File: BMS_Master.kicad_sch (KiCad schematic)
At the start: 70 parts, among them J1 PWR, J2 PROG, J3 BMS_M_OUT, J4 BMS_M_IN, J5 CAN, Q1 BC807, SW1 SW_SPST, U1 AP2204K-ADJ, U2 AP2204K-ADJ, U3 STM32F103C8Tx, U4 BQ79600-Q1, U5 SN65HVD256D, Y1 8M, Y2 32.768k

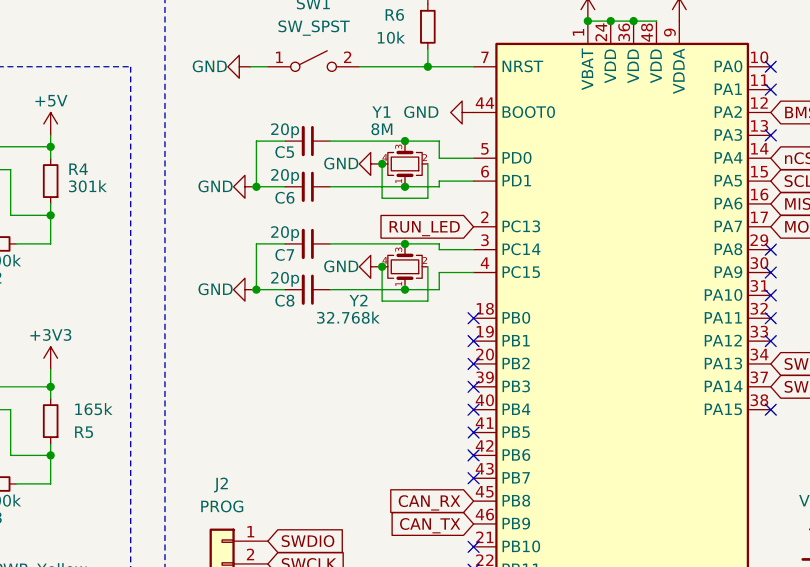
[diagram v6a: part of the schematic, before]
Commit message: Fix crystal pinout connection
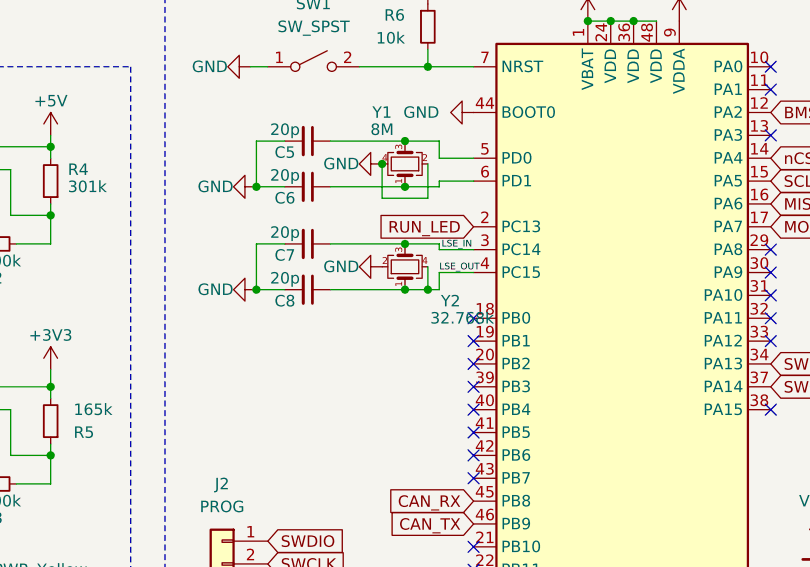
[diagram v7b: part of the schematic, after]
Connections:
- net GND: no longer Y2.4
- net LSE_OUT: now reaches C8.1, U3.4 (PC15), Y2.1
- net LSE_OUT: now also Y2.4
- net LSE_IN: now reaches C7.1, U3.3 (PC14), Y2.3
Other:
- moved on the sheet: Y2
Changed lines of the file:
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@@
   (junction (at 217.17 55.88) (diameter 0) (color 0 0 0 0)
   )
+  (junction (at 98.425 55.88) (diameter 0) (color 0 0 0 0)
+  )
   (junction (at 43.815 50.8) (diameter 0) (color 0 0 0 0)
   )
@@
   )
   (junction (at 219.71 135.89) (diameter 0) (color 0 0 0 0)
-  )
-  (junction (at 93.345 53.34) (diameter 0) (color 0 0 0 0)
   )
   (junction (at 204.47 71.12) (diameter 0) (color 0 0 0 0)
@@
     (stroke (width 0) (type default))
   )
-  (wire (pts (xy 95.885 55.88) (xy 99.695 55.88))
+  (wire (pts (xy 95.885 55.88) (xy 98.425 55.88))
     (stroke (width 0) (type default))
   )
@@
     (stroke (width 0) (type default))
   )
+  (wire (pts (xy 98.425 53.34) (xy 98.425 55.88))
+    (stroke (width 0) (type default))
+  )
   (wire (pts (xy 99.695 51.435) (xy 103.505 51.435))
     (stroke (width 0) (type default))
@@
     (stroke (width 0) (type default))
   )
+  (wire (pts (xy 98.425 55.88) (xy 99.695 55.88))
+    (stroke (width 0) (type default))
+  )
   (wire (pts (xy 106.68 162.56) (xy 106.68 164.465))
     (stroke (width 0) (type default))
@@
     (stroke (width 0) (type default))
   )
-  (wire (pts (xy 98.425 57.15) (xy 93.345 57.15))
-    (stroke (width 0) (type default))
-  )
   (wire (pts (xy 26.67 69.215) (xy 26.67 66.675))
     (stroke (width 0) (type default))
@@
     (stroke (width 0) (type default))
   )
+  (wire (pts (xy 87.63 55.88) (xy 95.885 55.88))
+    (stroke (width 0) (type default))
+  )
   (wire (pts (xy 43.815 40.005) (xy 56.515 40.005))
     (stroke (width 0) (type default))
@@
     (stroke (width 0) (type default))
   )
-  (wire (pts (xy 87.63 55.88) (xy 95.885 55.88))
-    (stroke (width 0) (type default))
-  )
   (wire (pts (xy 201.295 23.495) (xy 204.47 23.495))
     (stroke (width 0) (type default))
@@
     (stroke (width 0) (type default))
   )
-  (wire (pts (xy 93.345 57.15) (xy 93.345 53.34))
-    (stroke (width 0) (type default))
-  )
   (wire (pts (xy 27.305 42.545) (xy 26.67 42.545))
     (stroke (width 0) (type default))
@@
   )
   (wire (pts (xy 34.925 76.835) (xy 34.925 77.47))
-    (stroke (width 0) (type default))
-  )
-  (wire (pts (xy 98.425 53.34) (xy 98.425 57.15))
     (stroke (width 0) (type default))
   )
@@
   (text "MCU" (at 169.545 112.395 0)
     (effects (font (face "KiCad Font") (size 2.54 2.54) (thickness 0.508) bold) (justify left bottom))
+  )
+  (label "LSE_IN" (at 99.949 51.435 0) (fields_autoplaced)
+    (effects (font (size 0.735 0.735)) (justify left bottom))
+  )
+  (label "LSE_OUT" (at 99.695 53.975 0) (fields_autoplaced)
+    (effects (font (size 0.735 0.735)) (justify left bottom))
   )
   (global_label "BMS_FAULT" (shape input) (at 246.38 133.35 180) (fields_autoplaced)
@@
     )
   )
-  (symbol (lib_id "Device:Crystal_GND24_Small") (at 95.885 53.34 90) (unit 1)
-    (in_bom yes) (on_board yes) (dnp no)
-    (property "Reference" "Y2" (at 90.805 57.15 90)
-      (effects (font (size 1.27 1.27)))
-    )
-    (property "Value" "32.768k" (at 89.535 59.055 90)
-      (effects (font (size 1.27 1.27)))
-    )
+  (symbol (lib_id "Device:Crystal_GND24_Small") (at 95.885 53.34 270) (mirror x) (unit 1)
+    (in_bom yes) (on_board yes) (dnp no)
+    (property "Reference" "Y2" (at 100.965 57.15 90)
+      (effects (font (size 1.27 1.27)))
+    )
+    (property "Value" "32.768k" (at 102.235 59.055 90)
+      (effects (font (size 1.27 1.27)))
+    )

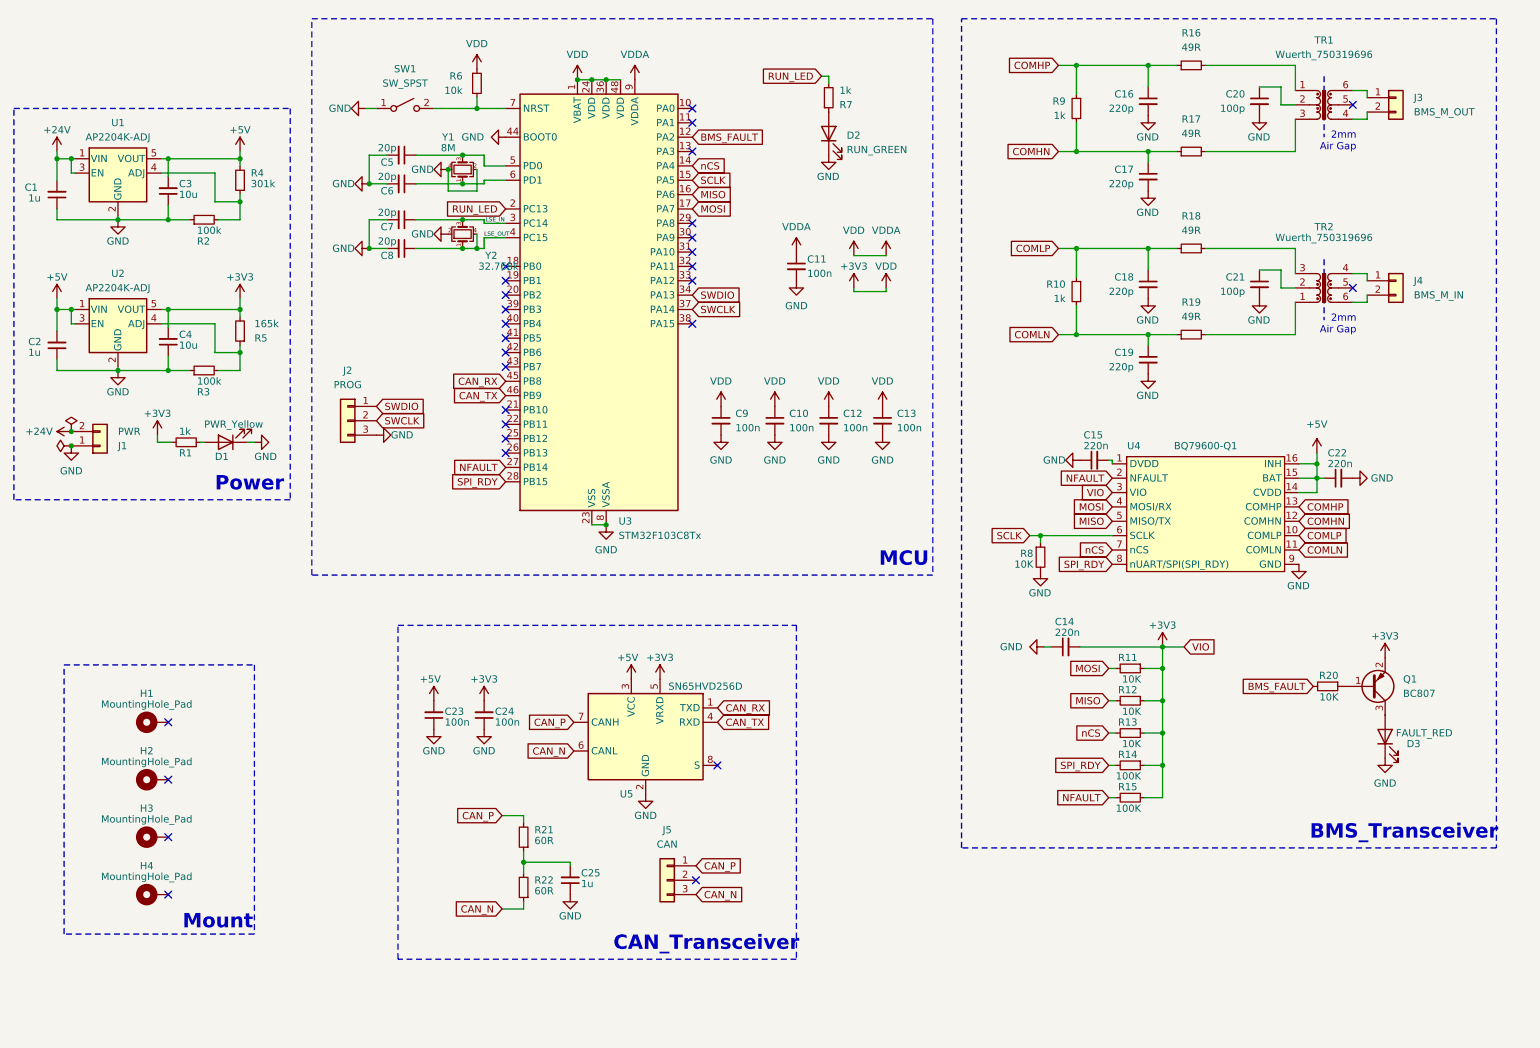
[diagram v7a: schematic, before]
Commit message: Add current sensor ADC port
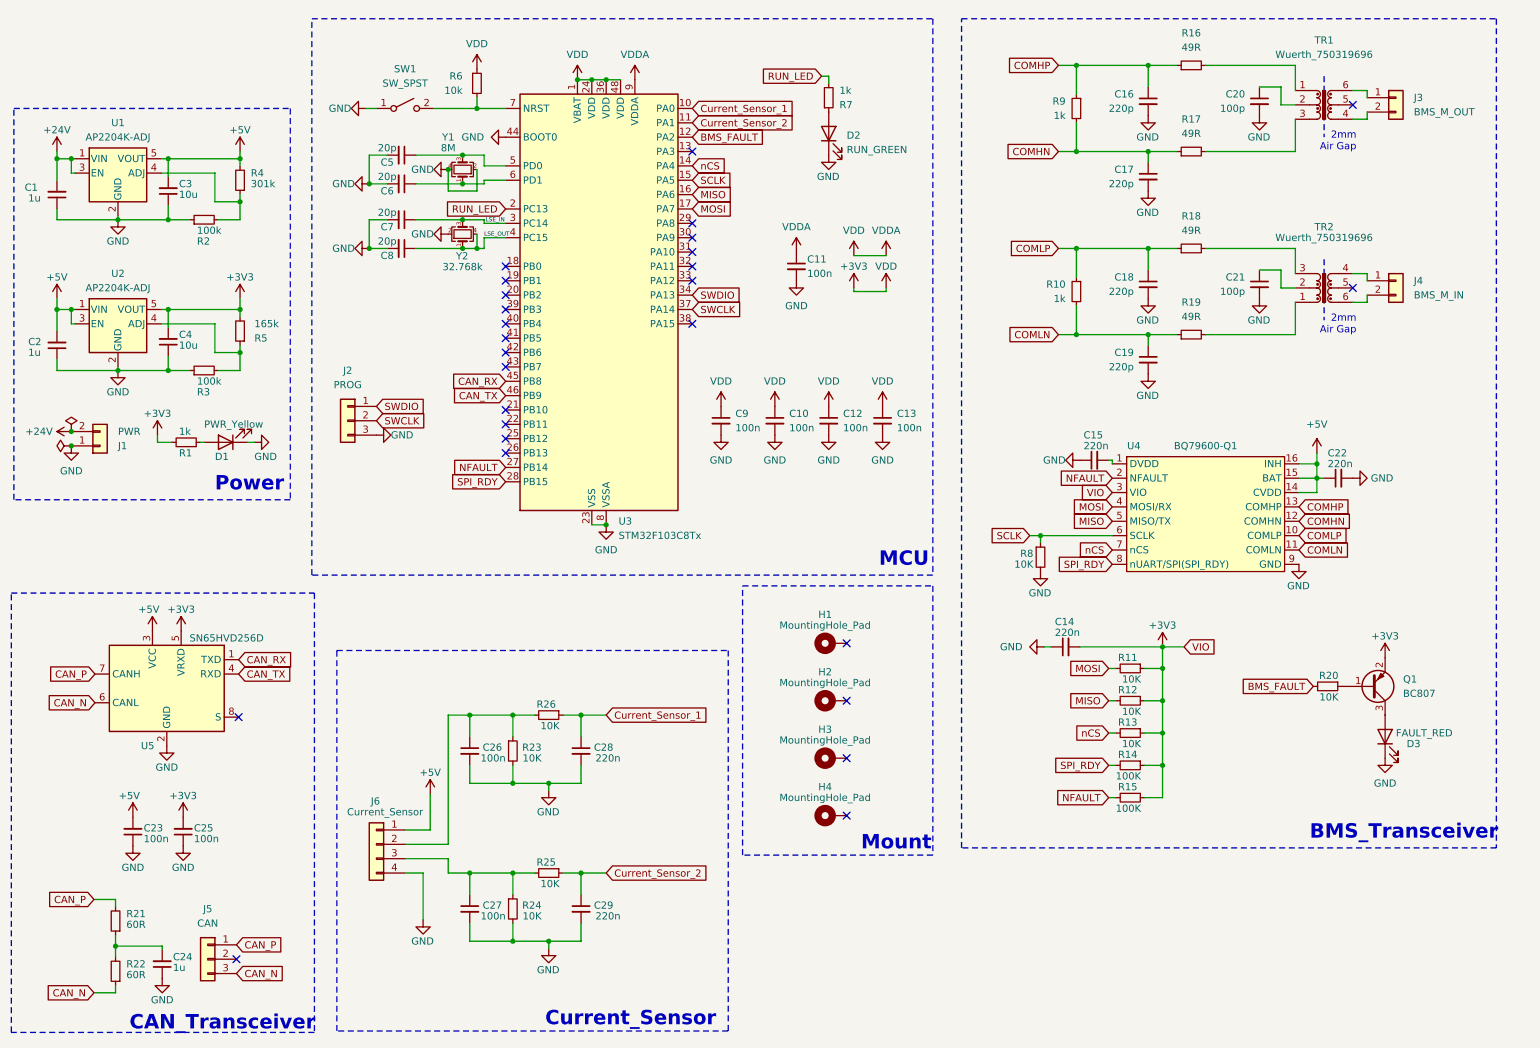
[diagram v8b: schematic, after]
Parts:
- added C26, C27: 100n, Capacitor_SMD:C_0603_1608Metric, symbol Device:C_Small
- added C28, C29: 220n, Capacitor_SMD:C_0805_2012Metric, symbol Device:C_Small
- added J6: Current_Sensor, symbol Connector_Generic:Conn_01x04
- added R23, R24, R25, R26: 10K, Resistor_SMD:R_0603_1608Metric, symbol Device:R_Small
- renumbered C25 to C24, C24 to C25
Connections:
- net +5V: now also J6.1 (Pin_1)
- net GND: now also C26.2, C27.2, C28.2, C29.2, J6.4 (Pin_4), R23.2, R24.2
- net Current_Sensor_1: now reaches U3.10 (PA0)
- net Current_Sensor_1: now also C28.1, R26.1
- net Current_Sensor_2: now reaches U3.11 (PA1)
- net Current_Sensor_2: now also C29.1, R25.1
- new net: C26.1, J6.2 (Pin_2), R23.1, R26.2
- new net: C27.1, J6.3 (Pin_3), R24.1, R25.2
- no-connect marks 29 -> 27
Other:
- note added: "Current_Sensor"
- moved on the sheet: C23, C24, C25, H1, H2, H3, H4, J5, R21, R22, U5
